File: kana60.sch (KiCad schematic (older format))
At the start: 136 parts, among them SW1 SW_PUSH, SW10 SW_PUSH, SW11 SW_PUSH, SW12 SW_PUSH, SW13 SW_PUSH, SW14 SW_PUSH, SW15 SW_PUSH, SW16 SW_PUSH, SW17 SW_PUSH, SW18 SW_PUSH, SW19 SW_PUSH, SW2 SW_PUSH, SW20 SW_PUSH, SW21 SW_PUSH, SW22 SW_PUSH, SW23 SW_PUSH, SW24 SW_PUSH, SW25 SW_PUSH, SW26 SW_PUSH, SW27 SW_PUSH, SW28 SW_PUSH, SW29 SW_PUSH, SW3 SW_PUSH, SW30 SW_PUSH, SW31 SW_PUSH, SW32 SW_PUSH, SW33 SW_PUSH, SW34 SW_PUSH, SW35 SW_PUSH, SW36 SW_PUSH, SW37 SW_PUSH, SW38 SW_PUSH, SW39 SW_PUSH, SW4 SW_PUSH, SW40 SW_PUSH, SW41 SW_PUSH, SW42 SW_PUSH, SW43 SW_PUSH, SW44 SW_PUSH, SW45 SW_PUSH, SW46 SW_PUSH, SW47 SW_PUSH, SW48 SW_PUSH, SW49 SW_PUSH, SW5 SW_PUSH, SW50 SW_PUSH, SW51 SW_PUSH, SW52 SW_PUSH, SW53 SW_PUSH, SW54 SW_PUSH, SW55 SW_PUSH, SW56 SW_PUSH, SW57 SW_PUSH, SW58 SW_PUSH, SW59 SW_PUSH, SW6 SW_PUSH, SW60 SW_PUSH, SW61 SW_PUSH, SW62 SW_PUSH, SW63 SW_PUSH, SW64 SW_PUSH, SW65 SW_PUSH, SW66 SW_PUSH, SW67 SW_PUSH, SW68 SW_PUSH, SW7 SW_PUSH, SW8 SW_PUSH, SW9 SW_PUSH, U1 ProMicro

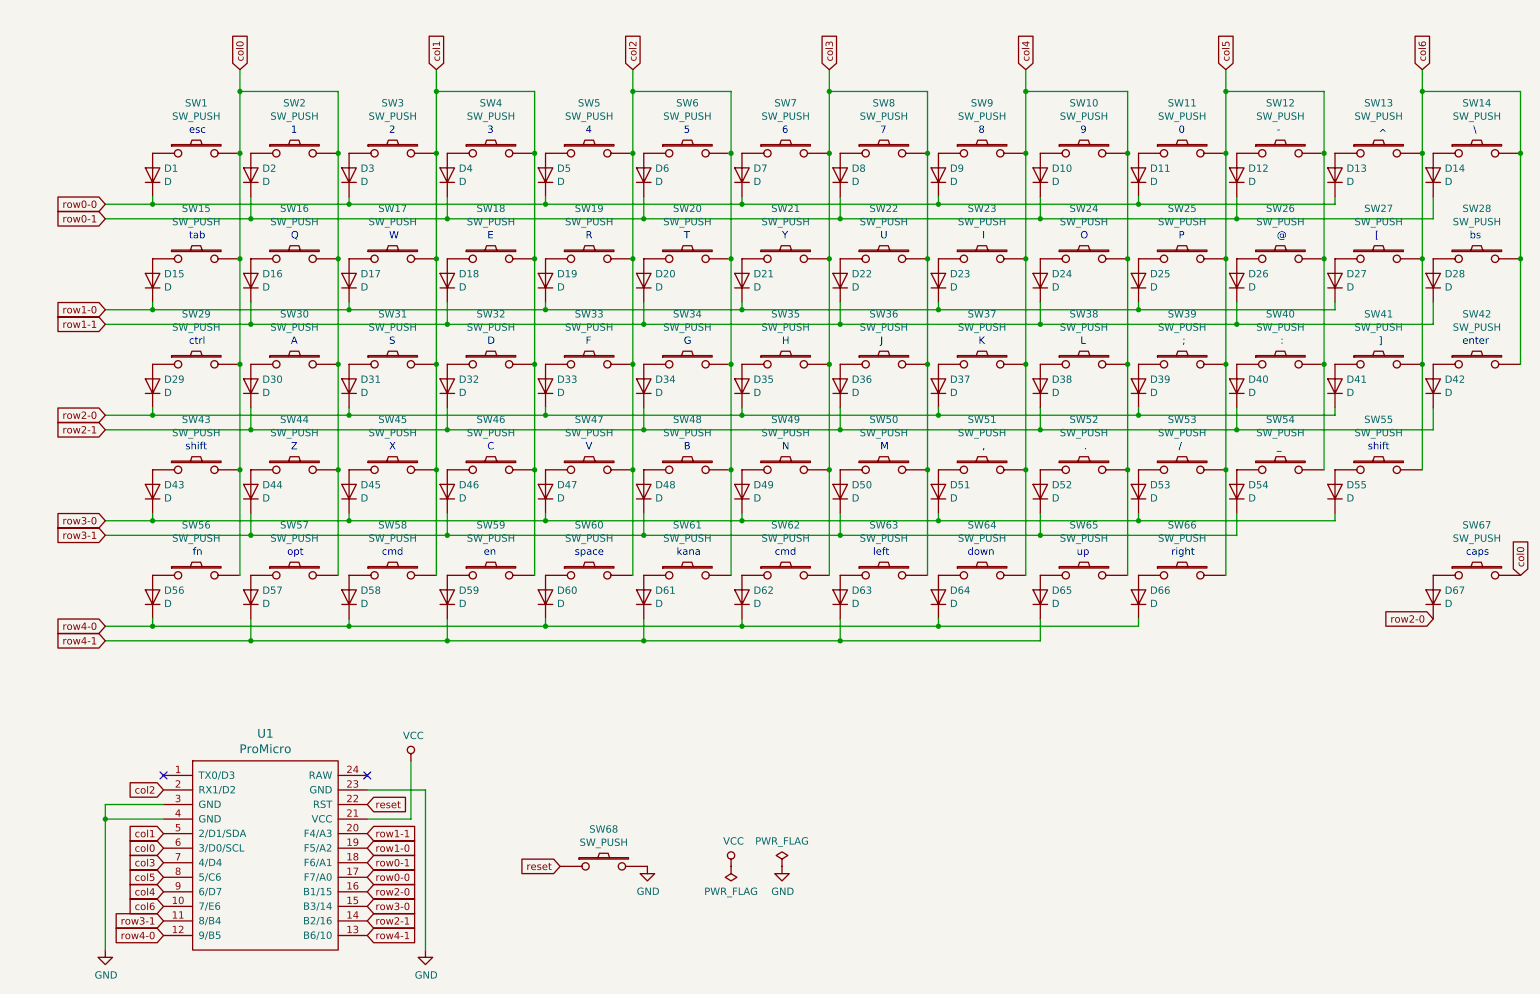
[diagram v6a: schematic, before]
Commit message: remove extra diode
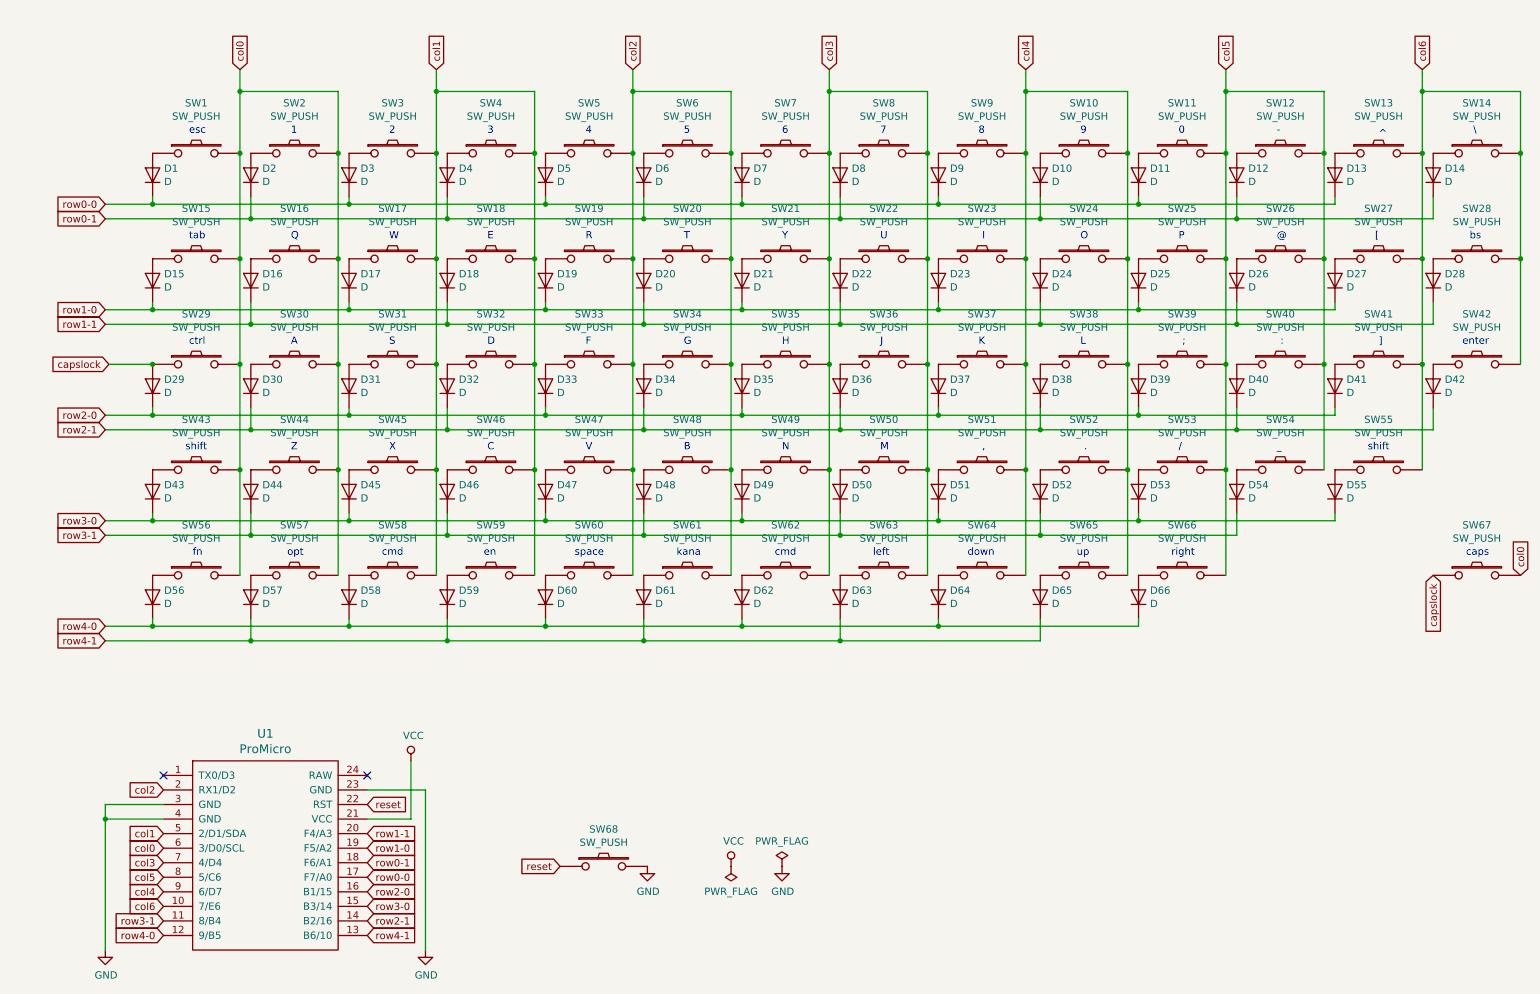
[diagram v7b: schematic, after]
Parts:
- removed D67: D, kbd:D3_TH_SMD, symbol Device:D
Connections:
- net capslock: now reaches D29.2 (A), SW29.1
- net capslock: now also SW67.1
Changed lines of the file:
@@
 	1    0    0    -1
-$EndComp
-$Comp
-L Device:D D67
-U 1 1 5D963060
-P 10250 4525
-F 0 "D67" V 10296 4446 50  0000 R CNN
-F 1 "D" V 10205 4446 50  0000 R CNN
-F 2 "kbd:D3_TH_SMD" H 10250 4525 50  0001 C CNN
-F 3 "~" H 10250 4525 50  0001 C CNN
-	1    10250 4525
-	0    -1   -1   0
 $EndComp
 Text GLabel 10850 4375 1    50   Input ~ 0
 col0
-Text GLabel 10250 4675 0    50   Input ~ 0
-row2-0
 NoConn ~ 1525 5750
 Text GLabel 1525 6450 0    50   Input ~ 0
@@
 Text Notes 9175 3525 0    50   ~ 0
 _
+Text GLabel 10250 4375 3    50   Input ~ 0
+capslock
+Text GLabel 1150 2925 0    50   Input ~ 0
+capslock
+Wire Wire Line
+	1150 2925 1450 2925
+Connection ~ 1450 2925
 $EndSCHEMATC

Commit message: change footprint
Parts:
- D1, D10, D11, D12, D13, D14, D15, D16, D17, D18, D19, D2, D20, D21, D22, D23, D24, D25, D26, D27, D28, D29, D3, D30, D31, D32, D33, D34, D35, D36, D37, D38, D39, D4, D40, D41, D42, D43, D44, D45, D46, D47, D48, D49, D5, D50, D51, D52, D53, D54, D55, D56, D57, D58, D59, D6, D60, D61, D62, D63, D64, D65, D66, D7, D8, D9: footprint kbd:D3_TH_SMD -> Keebio-Parts:Diode-dual
- SW1, SW10, SW11, SW12, SW13, SW14, SW15, SW16, SW17, SW18, SW19, SW2, SW20, SW21, SW22, SW23, SW24, SW25, SW26, SW27, SW28, SW29, SW3, SW30, SW31, SW32, SW33, SW34, SW35, SW36, SW37, SW38, SW39, SW4, SW40, SW41, SW42, SW43, SW44, SW45, SW46, SW47, SW48, SW49, SW5, SW50, SW51, SW52, SW53, SW54, SW55, SW56, SW57, SW58, SW59, SW6, SW60, SW61, SW62, SW63, SW64, SW65, SW66, SW67, SW7, SW8, SW9: footprint kbd:CherryMX_Choc_1u -> Keebio-Parts:MX-Alps-Choc-1U-NoLED
